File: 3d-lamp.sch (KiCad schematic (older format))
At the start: 15 parts

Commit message: Switch to ATTiny
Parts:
- removed BT?: Battery_Cell, symbol Battery_Cell
- removed U?: LPC1110FD20, symbol LPC1110FD20
- added BT1: Battery_Cell, symbol Battery_Cell
- added D10, D11: D_Zener, symbol D_Zener_Small
- added J1: USB, symbol USB
- added Q1: Q_NMOS_GDS, symbol Q_NMOS_GDS
- added R4, R5: 68, symbol R
- added R6: 10K, symbol R
- added U1: ATTINY85-10SU, Housings_SOIC:SOIC-8_3.9x4.9mm_Pitch1.27mm, symbol ATTINY85-10SU
- D1, D2, D3, D4, D5, D6, D7, D8, D9: renamed from D?; value LED_Small -> LED
- gave numbers to parts that had none: 4
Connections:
- net GND: now also BT1.2 (-), D10.2 (A), D11.2 (A), J1.1 (GND), U1.4 (GND)
- net at D1.2 (A), D4.2 (A), D7.2 (A): now also Q1.3 (S)
- net Vcc: now reaches C1.1
- net Vcc: now also BT1.1 (+), J1.2 (5V), Q1.2 (D), R6.1, U1.1 (PB5(~RESET~/dW/ADC0/PCINT5)), U1.8 (VCC)
- new net: Q1.1 (G), U1.6 (PB1(MISO/DO/AIN1/OC0B/OC1A/PCINT1))
- new net: D10.1 (K), J1.3 (USB_M), R5.2, R6.2
- new net: D11.1 (K), J1.4 (USB_P), R4.2
- new net PB3: R5.1, U1.2 (PB3(XTAL1/CLKI/~OC1B~/ADC3/PCINT3))
- new net PB4: R4.1, U1.3 (PB4(XTAL2/CLKO/OC1B/ADC2/PCINT4))
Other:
- moved on the sheet: C1, D1, D2, D3, D4, D5, D6, D7, D8, D9, R1, R2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

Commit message: Schema fertiggestellt
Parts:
- removed R3: R, symbol R
- added C2: 100nF, symbol C_Small
- added R1, R4, R5, R6, R7, R8, R9: 60Ω, symbol R
- added R10: 10K, symbol R
- added SW1: SW_SPST, symbol SW_SPST
- BT1: value Battery_Cell -> Battery_Cell (JST)
- C1: value C -> 100nF
- R2: value R -> 60Ω
- R3: renamed from R1; value R -> 60Ω
- U1: Digikey (none) -> ATTINY85V-10SURCT-ND
- renumbered R4 to R11, R5 to R12, R6 to R13
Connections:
- net GND: now also Q1.3 (S), C2.2, SW1.1 (A); no longer BT1.2 (-), R2.2, R3.2
- net Vcc: now also R2.1, R3.1, R1.1, R10.2, R4.1, R5.1, R6.1, R7.1, R8.1, R9.1; no longer Q1.2 (D), U1.1 (PB5(~RESET~/dW/ADC0/PCINT5))
- net at D1.1 (K): now also D2.1 (K), D3.1 (K), D4.1 (K), D5.1 (K), D6.1 (K), D7.1 (K), D8.1 (K), D9.1 (K), Q1.2 (D); no longer D2.2 (A)
- net at D3.2 (A): now also R3.2; no longer D2.1 (K)
- net at D5.2 (A): now also R5.2; no longer D4.1 (K)
- net at D6.2 (A): now also R6.2; no longer D5.1 (K)
- net at D8.2 (A): now also R8.2; no longer D7.1 (K)
- net at D9.2 (A): now also R9.2; no longer D8.1 (K)
- new net: D1.2 (A), R1.2
- new net: D2.2 (A), R2.2
- new net: D4.2 (A), R4.2
- new net: D7.2 (A), R7.2
- new net: BT1.2 (-), SW1.2 (B)
- new net: C2.1, R10.1, U1.1 (PB5(~RESET~/dW/ADC0/PCINT5))
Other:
- note added: "Batterie"
- note added: "LEDs"
- note added: "Mikrokontroller"
- note added: "USB"
- moved on the sheet: BT1, C1, D1, D10, D11, D2, D3, D4, D5, D6, D7, D8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

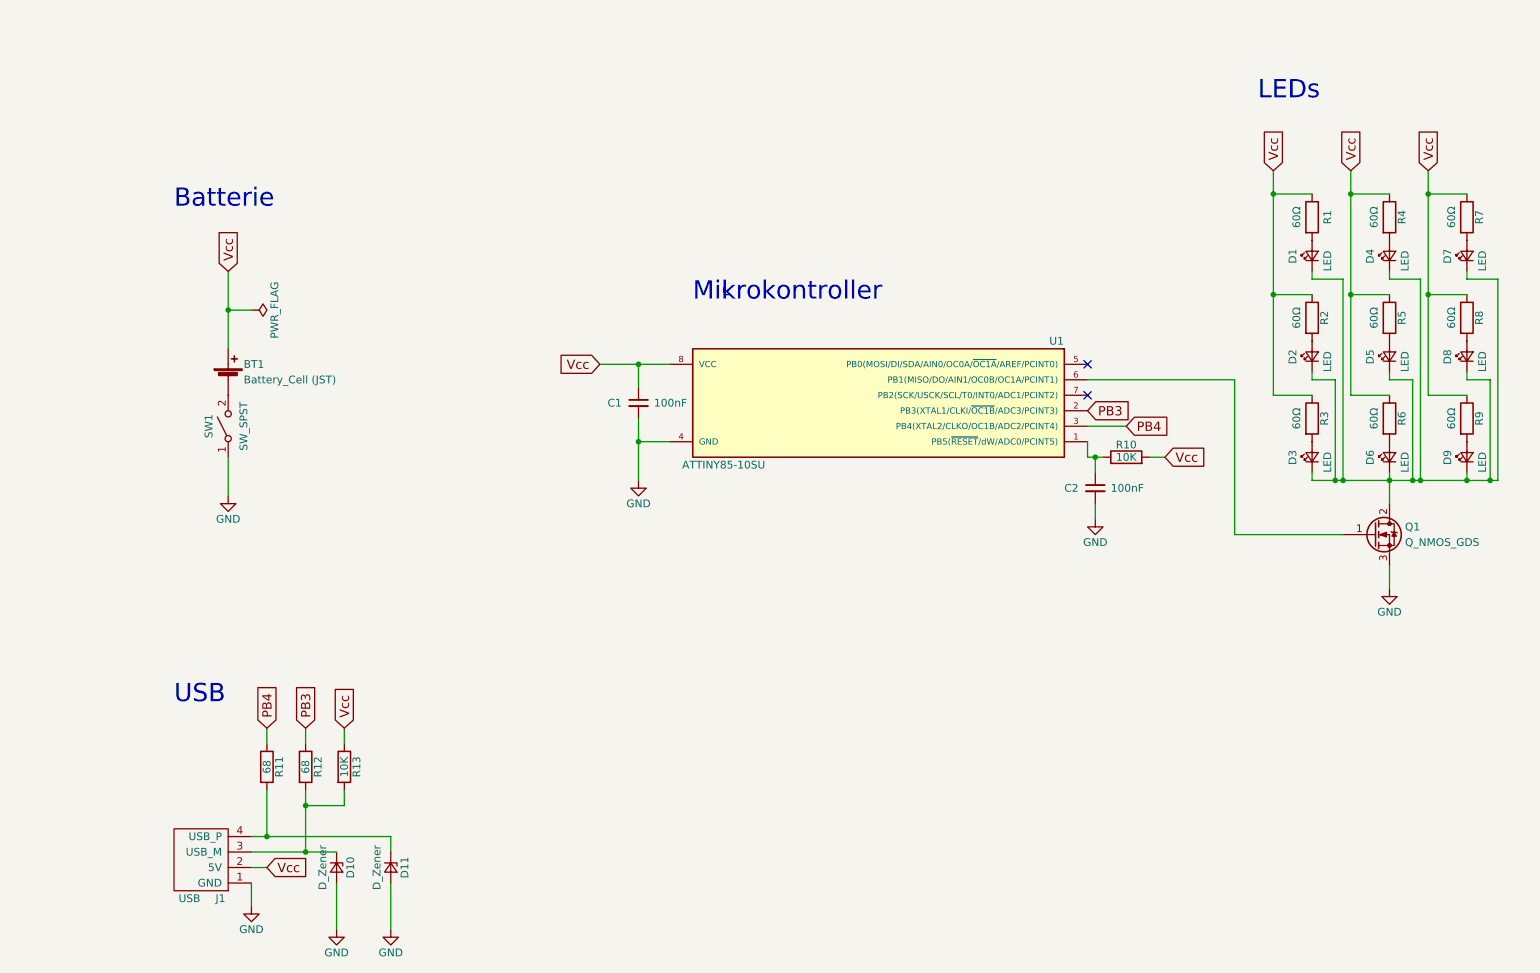
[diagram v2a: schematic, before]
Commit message: Remove USB from schematics
Instead, we'll program the uC externally.

Also add a debounced button.
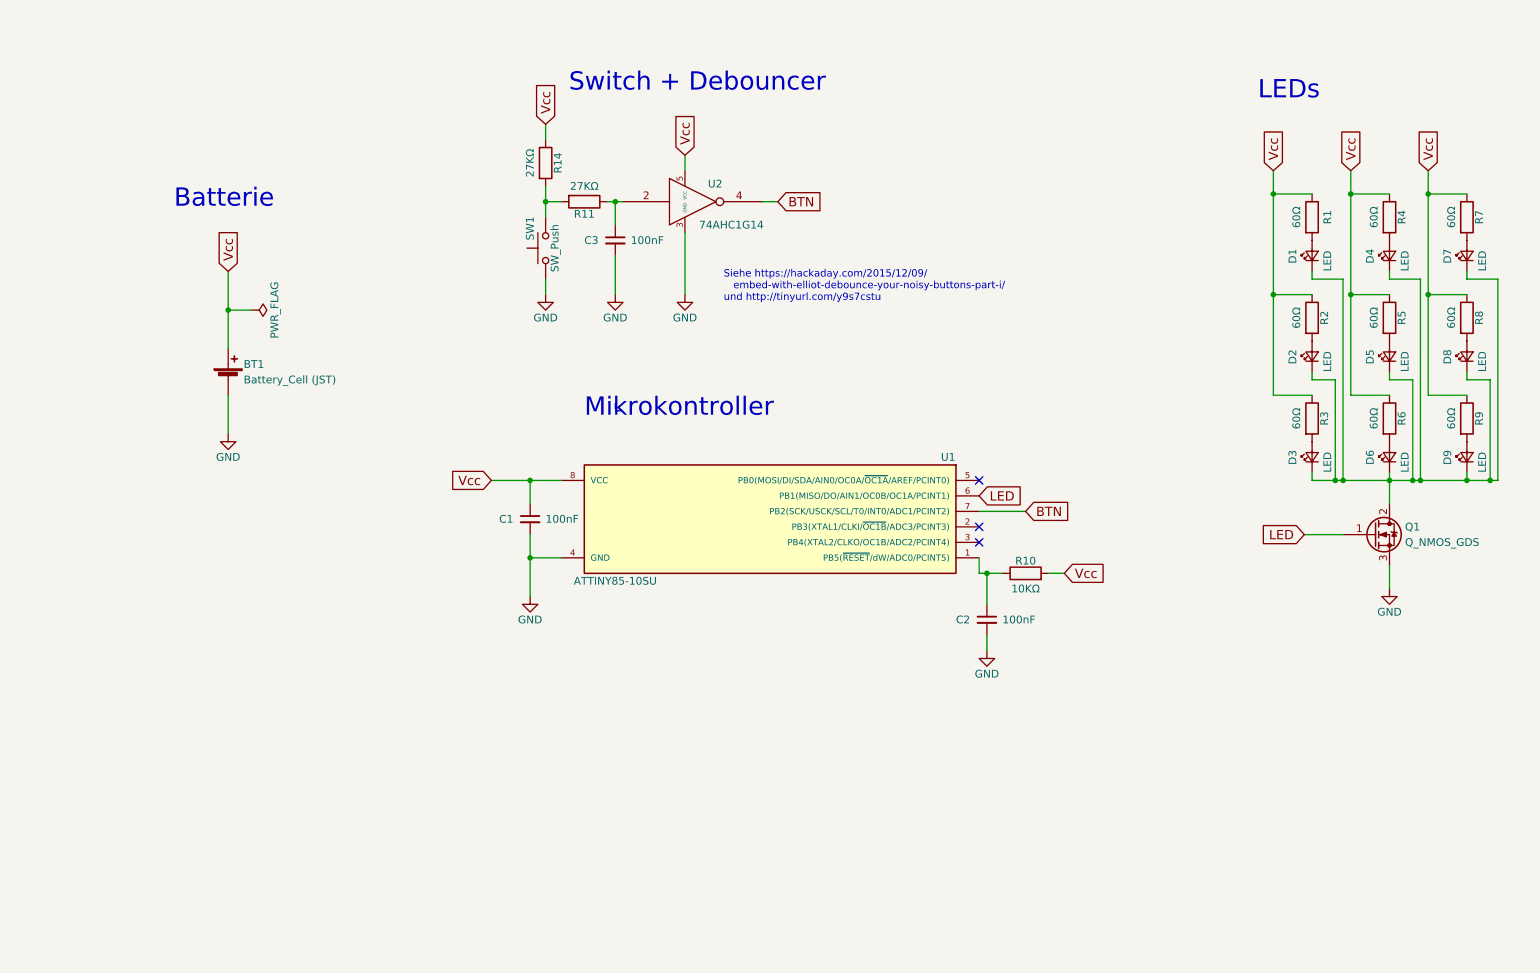
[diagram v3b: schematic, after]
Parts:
- removed D10, D11: D_Zener, symbol D_Zener_Small
- removed J1: USB, symbol USB
- removed R12: 68, symbol R
- removed R13: 10K, symbol R
- removed SW1: SW_SPST, symbol SW_SPST
- added C3: 100nF, Capacitors_SMD:C_1206_HandSoldering, symbol C_Small
- added R14: 27KΩ, Resistors_SMD:R_1206_HandSoldering, symbol R
- added SW1: SW_Push, symbol SW_Push
- added U2: 74AHC1G14, TO_SOT_Packages_SMD:SOT-353_SC-70-5_Handsoldering, symbol 74AHC1G14
- BT1: footprint (none) -> Socket_Strips:Socket_Strip_Straight_1x02_Pitch2.54mm
- C1, C2: footprint (none) -> Capacitors_SMD:C_1206_HandSoldering
- D1, D2, D3, D4, D5, D6, D7, D8, D9, R1, R2, R3, R4, R5, R6, R7, R8, R9: footprint (none) -> Resistors_SMD:R_1206_HandSoldering
- Q1: footprint (none) -> TO_SOT_Packages_SMD:SOT-223-3Lead_TabPin2
- R10: value 10K -> 10KΩ; footprint (none) -> Resistors_SMD:R_1206_HandSoldering
- R11: value 68 -> 27KΩ; footprint (none) -> Resistors_SMD:R_1206_HandSoldering
- U1: footprint Housings_SOIC:SOIC-8_3.9x4.9mm_Pitch1.27mm -> Housings_DIP:DIP-8_W7.62mm_Socket; Digikey ATTINY85V-10SURCT-ND -> ATTINY85-20PU-ND; Digikey_Socket (none) -> DILB8P-223TLF
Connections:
- net GND: now also BT1.2 (-), C3.2, SW1.1, U2.3 (GND)
- net Vcc: now also R14.1, U2.5 (VCC)
- net LED: now reaches Q1.1 (G), U1.6 (PB1(MISO/DO/AIN1/OC0B/OC1A/PCINT1))
- net at R11.2: now also R14.2, SW1.2
- net BTN: now reaches U1.7 (PB2(SCK/USCK/SCL/T0/INT0/ADC1/PCINT2))
- net BTN: now also U2.4
- net PB3: no longer names the net of U1.2 (PB3(XTAL1/CLKI/~OC1B~/ADC3/PCINT3))
- net PB4: no longer names the net of U1.3 (PB4(XTAL2/CLKO/OC1B/ADC2/PCINT4))
- net PB4: no longer R11.1
- new net: C3.1, R11.1, U2.2
- no-connect marks 2 -> 3
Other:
- note added: "Siehe https://hackaday.com/2015/12/09/\n embed-with-elliot-debounce-your-noisy-buttons-part-i/\nund http://tinyurl.com/y9s7cstu"
- note added: "Switch + Debouncer"
- note removed: "USB"
- moved on the sheet: C1, C2, R10, U1
